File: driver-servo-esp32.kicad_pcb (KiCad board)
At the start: 2 copper layers, 53.6 x 55.7 mm, 63 parts, among them J1 USB_B, J2 VCC, J3 Jack-DC, J4 GND, J5 USB_B, J6 PWM, Q1 Q_NPN_BEC, Q2 Q_NPN_BEC, SW1 SW_Push, SW2 SW_Push, SW3 SW_DIP_x01, SW4 SW_DIP_x01, U1 ESP32-PICO-D4, U2 CP2102N-SHORT, U3 AMS1117-3.3, U4 CP2102N-SHORT, U5 74HC245

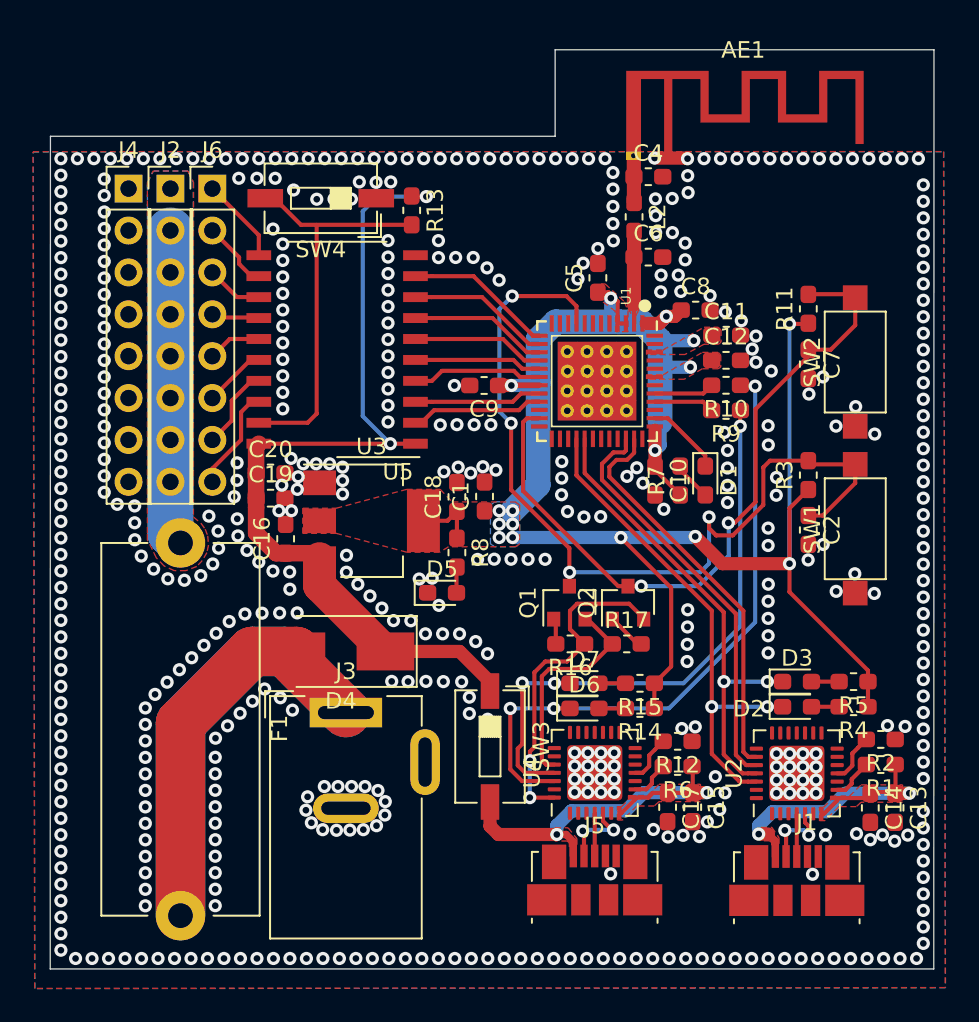
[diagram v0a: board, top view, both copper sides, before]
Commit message: fix reference of component - pcb
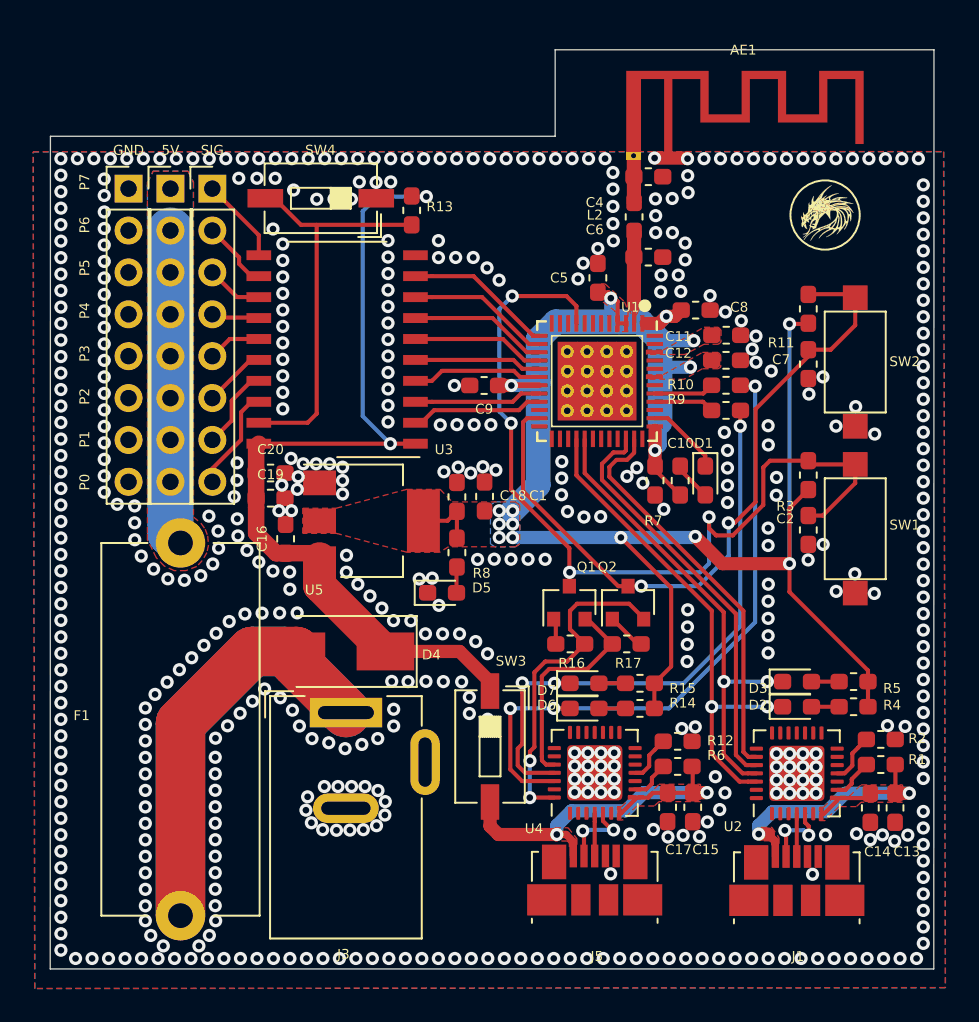
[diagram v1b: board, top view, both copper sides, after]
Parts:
- added OL1: Logo, footprints:Nam_logo, F.Cu at (139.7, 101.6)
- renumbered J2 to 5V, J4 to GND, J6 to SIG
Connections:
- U1 pad 10: (no net) -> Net-(U1-Pad10)
- U1 pad 11: (no net) -> Net-(U1-Pad11)
- U1 pad 12: (no net) -> Net-(U1-Pad12)
- U1 pad 22: (no net) -> Net-(U1-Pad22)
- U1 pad 24: (no net) -> Net-(U1-Pad24)
- U1 pad 25: (no net) -> Net-(U1-Pad25)
- U1 pad 26: (no net) -> Net-(U1-Pad26)
- U1 pad 27: (no net) -> Net-(U1-Pad27)
- U1 pad 30: (no net) -> Net-(U1-Pad30)
- U1 pad 31: (no net) -> Net-(U1-Pad31)
- U1 pad 32: (no net) -> Net-(U1-Pad32)
- U1 pad 33: (no net) -> Net-(U1-Pad33)
- U1 pad 36: (no net) -> Net-(U1-Pad36)
- U1 pad 39: (no net) -> Net-(U1-Pad39)
- U1 pad 42: (no net) -> Net-(U1-Pad42)
- U1 pad 44: (no net) -> Net-(U1-Pad44)
- U1 pad 45: (no net) -> Net-(U1-Pad45)
- U1 pad 47: (no net) -> Net-(U1-Pad47)
- U1 pad 48: (no net) -> Net-(U1-Pad48)
- U1 pad 5: (no net) -> Net-(U1-Pad5)
- U1 pad 6: (no net) -> Net-(U1-Pad6)
- U1 pad 7: (no net) -> Net-(U1-Pad7)
- U1 pad 8: (no net) -> Net-(U1-Pad8)
- U2 pad 1: (no net) -> Net-(U2-Pad1)
- U2 pad 10: (no net) -> Net-(U2-Pad10)
- U2 pad 12: (no net) -> Net-(U2-Pad12)
- U2 pad 13: (no net) -> Net-(U2-Pad13)
- U2 pad 14: (no net) -> Net-(U2-Pad14)
- U2 pad 15: (no net) -> Net-(U2-Pad15)
- U2 pad 16: (no net) -> Net-(U2-Pad16)
- U2 pad 17: (no net) -> Net-(U2-Pad17)
- U2 pad 18: (no net) -> Net-(U2-Pad18)
- U2 pad 19: (no net) -> Net-(U2-Pad19)
- U2 pad 2: (no net) -> Net-(U2-Pad2)
- U2 pad 20: (no net) -> Net-(U2-Pad20)
- U2 pad 21: (no net) -> Net-(U2-Pad21)
- U2 pad 22: (no net) -> Net-(U2-Pad22)
- U2 pad 27: (no net) -> Net-(U2-Pad27)
- U2 pad 28: (no net) -> Net-(U2-Pad28)
- U2 pad 6: (no net) -> Net-(U2-Pad6)
- U4 pad 1: (no net) -> Net-(U4-Pad1)
- U4 pad 10: (no net) -> Net-(U4-Pad10)
- U4 pad 12: (no net) -> Net-(U4-Pad12)
- U4 pad 13: (no net) -> Net-(U4-Pad13)
- U4 pad 14: (no net) -> Net-(U4-Pad14)
- U4 pad 15: (no net) -> Net-(U4-Pad15)
- U4 pad 16: (no net) -> Net-(U4-Pad16)
- U4 pad 17: (no net) -> Net-(U4-Pad17)
- U4 pad 18: (no net) -> Net-(U4-Pad18)
- U4 pad 19: (no net) -> Net-(U4-Pad19)
- U4 pad 2: (no net) -> Net-(U4-Pad2)
- U4 pad 20: (no net) -> Net-(U4-Pad20)
- U4 pad 21: (no net) -> Net-(U4-Pad21)
- U4 pad 22: (no net) -> Net-(U4-Pad22)
- U4 pad 23: (no net) -> Net-(U4-Pad23)
- U4 pad 27: (no net) -> Net-(U4-Pad27)
- U4 pad 6: (no net) -> Net-(U4-Pad6)
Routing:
- net GND: vias 506 -> 520
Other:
- board text added: "P0"
- board text added: "P1"
- board text added: "P2"
- board text added: "P3"
- board text added: "P4"
- board text added: "P5"
- board text added: "P6"
- board text added: "P7"

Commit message: export gerber
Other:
- board size 53.6 x 55.7 mm -> 55 x 55.9 mm
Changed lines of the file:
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@@
     (35 F.Paste user hide)
     (36 B.SilkS user hide)
-    (37 F.SilkS user hide)
+    (37 F.SilkS user)
     (38 B.Mask user hide)
     (39 F.Mask user hide)
@@
     (45 Margin user hide)
     (46 B.CrtYd user hide)
-    (47 F.CrtYd user hide)
+    (47 F.CrtYd user)
     (48 B.Fab user hide)
     (49 F.Fab user hide)
@@
       (outputformat 1)
       (mirror false)
-      (drillshape 1)
+      (drillshape 0)
       (scaleselection 1)
-      (outputdirectory ""))
+      (outputdirectory "asset/"))
   )
   (net 0 "")
@@
     (descr "Through hole straight pin header, 1x08, 2.54mm pitch, single row")
     (tags "Through hole pin header THT 1x08 2.54mm single row")
-    (fp_text reference 5V (at 0 -2.33) (layer F.SilkS)
+    (fp_text reference 5V (at 0 20) (layer F.SilkS)
       (effects (font (size 0.6 0.6) (thickness 0.15)))
     )
@@
     (tags "PCB antenna")
     (attr virtual)
-    (fp_text reference AE1 (at 4.55 -6.41) (layer F.SilkS)
+    (fp_text reference AE1 (at 4.55 -1.0059) (layer F.SilkS)
       (effects (font (size 0.6 0.6) (thickness 0.15)))
     )
@@
     (tags "capacitor handsolder")
     (attr smd)
-    (fp_text reference C5 (at 0 -2.3495 180) (layer F.SilkS)
+    (fp_text reference C5 (at 0.01 -2.1205 180) (layer F.SilkS)
       (effects (font (size 0.6 0.6) (thickness 0.15)))
     )
@@
     (tags "capacitor handsolder")
     (attr smd)
-    (fp_text reference C16 (at 0 -1.43 90) (layer F.SilkS)
+    (fp_text reference C16 (at 0.7342 -1.43 90) (layer F.SilkS)
       (effects (font (size 0.6 0.6) (thickness 0.15)))
     )
@@
     (tags "LED handsolder")
     (attr smd)
-    (fp_text reference D1 (at -2.255601 0.100799 180) (layer F.SilkS)
+    (fp_text reference D1 (at -2.255601 -0.165201 180) (layer F.SilkS)
       (effects (font (size 0.6 0.6) (thickness 0.15)))
     )
@@
     (tags "LED handsolder")
     (attr smd)
-    (fp_text reference D6 (at -2.2987 -0.2032) (layer F.SilkS)
+    (fp_text reference D6 (at -2.5077 -0.2032) (layer F.SilkS)
       (effects (font (size 0.6 0.6) (thickness 0.15)))
     )
@@
     (tags "LED handsolder")
     (attr smd)
-    (fp_text reference D7 (at -2.2987 0.4318) (layer F.SilkS)
+    (fp_text reference D7 (at -2.5077 0.4318) (layer F.SilkS)
       (effects (font (size 0.6 0.6) (thickness 0.15)))
     )
@@
     (tags "Micro B USB SMD")
     (attr smd)
-    (fp_text reference J1 (at 0.0658 4.5982 180) (layer F.SilkS)
+    (fp_text reference J1 (at 0.0168 4.5402 180) (layer F.SilkS)
       (effects (font (size 0.6 0.6) (thickness 0.15)))
     )
@@
     (descr "Through hole straight pin header, 1x08, 2.54mm pitch, single row")
     (tags "Through hole pin header THT 1x08 2.54mm single row")
-    (fp_text reference GND (at 0 -2.33) (layer F.SilkS)
+    (fp_text reference GND (at -0.96 20) (layer F.SilkS)
       (effects (font (size 0.6 0.6) (thickness 0.15)))
     )
@@
     (tags "Micro B USB SMD")
     (attr smd)
-    (fp_text reference J5 (at 0.1272 4.6296 180) (layer F.SilkS)
+    (fp_text reference J5 (at 0.1272 4.5716 180) (layer F.SilkS)
       (effects (font (size 0.6 0.6) (thickness 0.15)))
     )
@@
     (descr "Through hole straight pin header, 1x08, 2.54mm pitch, single row")
     (tags "Through hole pin header THT 1x08 2.54mm single row")
-    (fp_text reference SIG (at 0 -2.33) (layer F.SilkS)
+    (fp_text reference SIG (at 0.46 20) (layer F.SilkS)
       (effects (font (size 0.6 0.6) (thickness 0.15)))
     )
@@
     (tags "SMD DIP Switch SPST Slide 6.73mm 264mil SMD LowProfile JPin")
     (attr smd)
-    (fp_text reference SW4 (at 0.0254 2.921) (layer F.SilkS)
+    (fp_text reference SW4 (at -5.8816 1.584) (layer F.SilkS)
       (effects (font (size 0.6 0.6) (thickness 0.15)))
     )
@@
     (effects (font (size 0.6 0.6) (thickness 0.15)))
   )
-  (gr_line (start 123.3297 91.5797) (end 146.304 91.5797) (layer Edge.Cuts) (width 0.05))
-  (gr_line (start 123.3297 96.825) (end 123.3297 91.5797) (layer Edge.Cuts) (width 0.05))
-  (gr_line (start 92.7227 96.825) (end 123.3297 96.825) (layer Edge.Cuts) (width 0.05))
-  (gr_line (start 92.71 147.32) (end 92.7227 96.825) (layer Edge.Cuts) (width 0.05))
-  (gr_line (start 146.2913 147.32) (end 92.71 147.32) (layer Edge.Cuts) (width 0.05))
-  (gr_line (start 146.304 91.5797) (end 146.2913 147.32) (layer Edge.Cuts) (width 0.05))
+  (gr_line (start 123.3297 91.5797) (end 147 91.5797) (layer Edge.Cuts) (width 0.05))
+  (gr_line (start 123.3297 97.5) (end 123.3297 91.5797) (layer Edge.Cuts) (width 0.05))
+  (gr_line (start 92 97.5) (end 123.3297 97.5) (layer Edge.Cuts) (width 0.05))
+  (gr_line (start 91.9988 147.5) (end 92 97.5) (layer Edge.Cuts) (width 0.05))
+  (gr_line (start 147 147.5) (end 92 147.5) (layer Edge.Cuts) (width 0.05))
+  (gr_line (start 147 91.5797) (end 147 147.5) (layer Edge.Cuts) (width 0.05))
   (via (at 131.0132 132.7404) (size 0.8) (drill 0.4) (layers F.Cu B.Cu) (net 1))
   (via (at 131.826 132.6388) (size 0.8) (drill 0.4) (layers F.Cu B.Cu) (net 1))
